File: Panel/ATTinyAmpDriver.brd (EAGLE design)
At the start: 50 x 50 mm, 44 parts, among them Q1 SI2301CDS, Q2 BC846, U1 SPX5205M5-L-3-3, U2 ATTINY5-TSHR, U3 MCP6L2-X_SN

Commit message: Turn and Tail combined Panel
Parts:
- removed LED10, LED11, LED12, LED5, LED6, LED7, LED8, LED9: LUXEON_REBELCREE_XP-E, Combined:CREE_XP-E
- removed X1, X2: (no value), con-phoenix-254:2POL254
- moved U$1 35.3 mm to (5.33, 7.92), turned to 90 degrees
- moved LED3 35.3 mm to (37.7, 13.2), flipped to the bottom, turned to 180 degrees
- moved Q1 35.0 mm to (31.1, 2.59), turned to 270 degrees
- moved C1 33.9 mm to (13.6, 3.63), turned to 180 degrees
- moved R2 33.2 mm to (25.5, 2.51), turned to 90 degrees
- moved R1 31.5 mm to (22.8, 3.58), turned to 0 degrees
- moved C6 31.3 mm to (19.1, 4.01), turned to 270 degrees
- moved PWM 31.1 mm to (29.1, 4.80), turned to 0 degrees
- moved TPIDATA 31.0 mm to (20.6, 4.01), turned to 0 degrees
- moved C3 30.9 mm to (16.8, 4.78), turned to 270 degrees
- moved Q2 30.3 mm to (27.1, 4.85), turned to 180 degrees
- moved U1 30.2 mm to (13.5, 6.53), turned to 0 degrees
- moved +5V 29.4 mm to (15.2, 6.48), turned to 0 degrees
- moved RESET 28.8 mm to (20.6, 5.61), turned to 0 degrees
- moved C5 27.7 mm to (23.5, 6.30), turned to 180 degrees
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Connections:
- removed net N$1 (its old number): LED5.AN, LED6.CT
- removed net N$13: LED11.CT, LED12.AN
- removed net N$14: LED9.AN, Q1.P$3
- removed net N$15: LED10.AN, LED9.CT
- removed net N$2 (its old number): LED1.AN, LED2.CT
- removed net N$4 (its old number): LED3.AN, LED4.CT
- removed net N$5 (its old number): LED6.AN, LED7.CT
- removed net N$6 (its old number): LED7.AN, LED8.CT
- removed net THERMAL: LED1.TH, LED2.TH, LED3.TH, LED4.TH
- removed net THERMAL1: LED5.TH, LED6.TH, LED7.TH, LED8.TH
- removed net V+: LED4.AN, X1.1
- removed net V+1: LED8.AN, X2.1
- removed net V-: LED1.CT, X1.2
- removed net V-1: LED5.CT, X2.2
- new net N$10: LED3.CT, LED4.AN
- new net N$7: LED1.CT, LED2.AN
- net CROSSOVER: now also LED2.CT, LED3.AN; no longer LED10.CT, LED11.AN
- net D-: now also LED4.CT; no longer LED12.CT
- net GND: now also LED1.TH, LED2.TH, LED3.TH, LED4.TH; no longer LED10.TH, LED11.TH, LED12.TH, LED9.TH
- net N$3: now also LED1.AN, Q1.P$3; no longer LED2.AN, LED3.CT
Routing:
- net N$1 (its old number): track 15.1 -> 0.00 mm
- net N$2 (its old number): track 15.1 -> 0.00 mm
- net N$5 (its old number): track 11.7 -> 0.00 mm
- net N$6 (its old number): track 11.6 -> 0.00 mm
- net N$4 (its old number): track 11.6 -> 0.00 mm
- net N$3: track 11.7 -> 4.97 mm
- net V+1: track 6.39 -> 0.00 mm
- net V+: track 6.39 -> 0.00 mm
- net V-: track 5.81 -> 0.00 mm
- net V-1: track 5.81 -> 0.00 mm
- net N$14: track 4.97 -> 0.00 mm
- net N$7: track 0.00 -> 4.76 mm, vias 0 -> 1
- net N$15: track 4.76 -> 0.00 mm, vias 1 -> 0
- net N$10: track 0.00 -> 4.06 mm, vias 0 -> 1
- net N$13: track 4.06 -> 0.00 mm, vias 1 -> 0
- removed copper zone on layer 1, net THERMAL
- removed copper zone on layer 16, net THERMAL
- removed copper zone on layer 1, net THERMAL1
- removed copper zone on layer 16, net THERMAL1
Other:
- board size 50 x 50 mm -> 41.9 x 15.9 mm
- board text removed: "+"
- board text removed: "-"
- board text removed: "EM20130714"

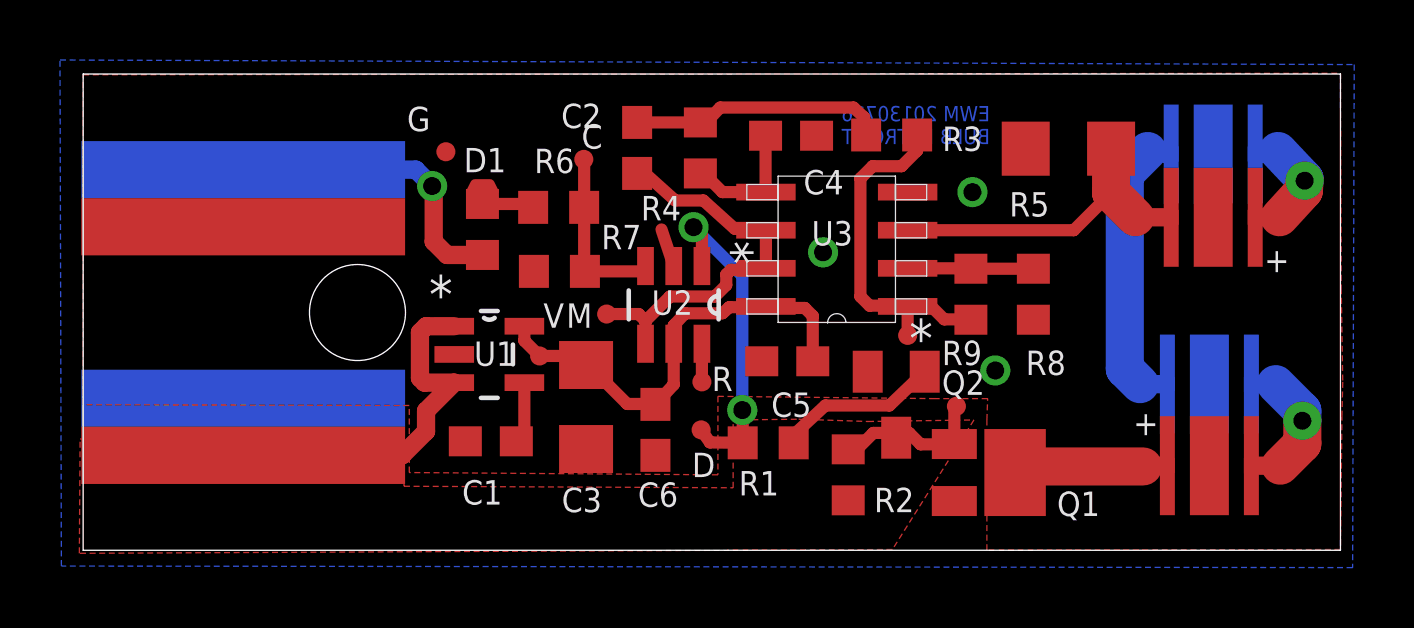
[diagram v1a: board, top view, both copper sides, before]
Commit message: updated tail board in combined panel
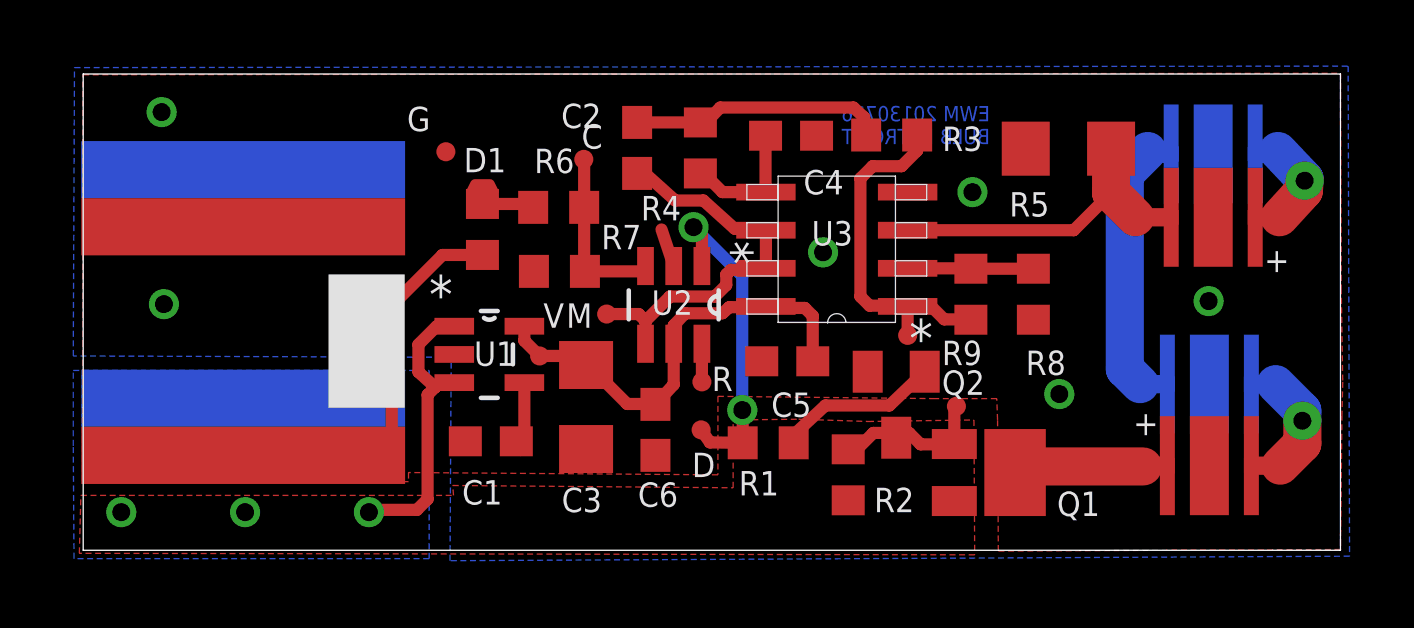
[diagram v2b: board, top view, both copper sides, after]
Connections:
- net +14V: now also U$1.L1; no longer U$1.H1
- net GND: now also U$1.H2; no longer U$1.L1
- net N$1: now also U$1.H1; no longer U$1.H2
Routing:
- net N$1: track 10.2 -> 13.6 mm, vias 1 -> 0
- net +14V: track 12.4 -> 9.79 mm, vias 0 -> 3
- net GND: vias 3 -> 6
- added copper zone on layer 16, net +14V
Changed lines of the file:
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@@
 <vertex x="41.9608" y="4.5212"/>
 <vertex x="41.91" y="0.0254"/>
-<vertex x="30.1244" y="0"/>
-<vertex x="30.1244" y="4.3434"/>
-<vertex x="30.1498" y="5.0546"/>
+<vertex x="30.5054" y="-0.0254"/>
+<vertex x="30.48" y="4.3434"/>
+<vertex x="30.4546" y="5.0546"/>
 <vertex x="28.3972" y="5.0546"/>
 <vertex x="21.1582" y="5.1308"/>
 <vertex x="21.1582" y="2.5146"/>
-<vertex x="10.8712" y="2.5908"/>
-<vertex x="10.8712" y="4.826"/>
-<vertex x="0" y="4.8514"/>
+<vertex x="10.8458" y="2.5908"/>
+<vertex x="10.8458" y="2.286"/>
+<vertex x="-0.0254" y="2.3114"/>
 </polygon>
 <polygon width="0.254" layer="16">
-<vertex x="-0.772" y="16.3422"/>
-<vertex x="42.369" y="16.1898"/>
-<vertex x="42.315" y="-0.5784"/>
-<vertex x="-0.726" y="-0.526"/>
+<vertex x="-0.2894" y="16.0882"/>
+<vertex x="42.1658" y="16.139"/>
+<vertex x="42.2134" y="-0.1974"/>
+<vertex x="12.228" y="-0.3482"/>
+<vertex x="12.2682" y="6.4336"/>
+<vertex x="-0.3302" y="6.477"/>
 </polygon>
 <contactref element="GND" pad="P$1"/>
@@
 <via x="24.6634" y="9.9314" extent="1-16" drill="0.6"/>
 <via x="29.6418" y="11.938" extent="1-16" drill="0.6"/>
-<via x="30.4038" y="5.9944" extent="1-16" drill="0.6"/>
+<via x="32.5374" y="5.207" extent="1-16" drill="0.6"/>
 <contactref element="LED1" pad="TH"/>
 <contactref element="LED4" pad="TH"/>
@@
 <contactref element="LED2" pad="TH"/>
 <contactref element="U$1" pad="L2"/>
-<contactref element="U$1" pad="L1"/>
+<contactref element="U$1" pad="H2"/>
+<via x="37.5158" y="8.3058" extent="1-16" drill="0.6"/>
+<via x="2.6162" y="14.605" extent="1-16" drill="0.6"/>
+<via x="2.6924" y="8.2042" extent="1-16" drill="0.6"/>
 </signal>
 <signal name="+14V">
@@
 <contactref element="U1" pad="3"/>
 <polygon width="0.254" layer="1">
-<vertex x="-0.1016" y="3.7084"/>
-<vertex x="10.7188" y="3.556"/>
-<vertex x="10.6934" y="2.1336"/>
+<vertex x="-0.0762" y="1.8288"/>
+<vertex x="12.3444" y="1.8288"/>
+<vertex x="12.319" y="2.159"/>
 <vertex x="21.6662" y="2.0828"/>
 <vertex x="21.6662" y="4.3434"/>
@@
 <vertex x="26.162" y="4.2926"/>
 <vertex x="29.6926" y="4.3434"/>
-<vertex x="26.9748" y="0.0254"/>
+<vertex x="29.718" y="-0.1524"/>
 <vertex x="-0.127" y="-0.1016"/>
 </polygon>
 <contactref element="Q1" pad="P$2"/>
 <contactref element="R2" pad="1"/>
-<contactref element="U$1" pad="H1"/>
-<wire x1="5.334" y1="3.1623" x2="10.6299" y2="3.1623" width="0.6096" layer="1"/>
-<wire x1="10.6299" y1="3.1623" x2="11.43" y2="3.9624" width="0.6096" layer="1"/>
-<wire x1="11.43" y1="3.9624" x2="11.43" y2="4.6482" width="0.6096" layer="1"/>
-<wire x1="11.43" y1="4.6482" x2="12.3698" y2="5.588" width="0.6096" layer="1"/>
-<wire x1="12.3698" y1="7.4676" x2="11.43" y2="7.4676" width="0.6096" layer="1"/>
-<wire x1="11.43" y1="7.4676" x2="11.2268" y2="7.2644" width="0.6096" layer="1"/>
-<wire x1="11.2268" y1="7.2644" x2="11.2268" y2="5.7404" width="0.6096" layer="1"/>
-<wire x1="11.2268" y1="5.7404" x2="11.3792" y2="5.588" width="0.6096" layer="1"/>
-<wire x1="11.3792" y1="5.588" x2="12.3698" y2="5.588" width="0.6096" layer="1"/>
-<wire x1="25.5016" y1="1.6646" x2="29.0392" y2="1.6408" width="0" layer="19" extent="1-1"/>
+<contactref element="U$1" pad="L1"/>
+<polygon width="0.3048" layer="16">
+<vertex x="-0.3302" y="5.9944"/>
+<vertex x="11.5316" y="5.9944"/>
+<vertex x="11.5316" y="-0.2794"/>
+<vertex x="-0.3048" y="-0.2794"/>
+<vertex x="-0.3302" y="3.4798"/>
+</polygon>
+<via x="1.27" y="1.27" extent="1-16" drill="0.6"/>
+<via x="5.3975" y="1.27" extent="1-16" drill="0.6"/>
+<via x="9.525" y="1.27" extent="1-16" drill="0.6"/>
+<wire x1="12.3698" y1="5.588" x2="11.8872" y2="5.588" width="0.4064" layer="1"/>
+<wire x1="11.8872" y1="5.588" x2="11.7348" y2="5.4356" width="0.4064" layer="1"/>
+<wire x1="11.7348" y1="5.4356" x2="11.4808" y2="5.1816" width="0.4064" layer="1"/>
+<wire x1="11.4808" y1="5.1816" x2="11.4808" y2="1.7018" width="0.4064" layer="1"/>
+<wire x1="11.4808" y1="1.7018" x2="11.1252" y2="1.3462" width="0.4064" layer="1"/>
+<wire x1="11.1252" y1="1.3462" x2="9.6012" y2="1.3462" width="0.4064" layer="1"/>
+<wire x1="9.6012" y1="1.3462" x2="9.525" y2="1.27" width="0.4064" layer="1"/>
+<wire x1="12.3698" y1="7.4676" x2="11.7856" y2="7.4676" width="0.4064" layer="1"/>
+<wire x1="11.7856" y1="7.4676" x2="11.176" y2="6.858" width="0.4064" layer="1"/>
+<wire x1="11.176" y1="6.858" x2="11.176" y2="5.9436" width="0.4064" layer="1"/>
+<wire x1="11.176" y1="5.9436" x2="11.7348" y2="5.4356" width="0.4064" layer="1"/>
 </signal>
 <signal name="VCC">
@@
 <signal name="N$1">
 <contactref element="D1" pad="1A"/>
-<contactref element="U$1" pad="H2"/>
-<via x="11.6332" y="12.1412" extent="1-16" drill="0.6" diameter="0.4064" shape="square"/>
-<wire x1="13.3096" y1="9.8434" x2="12.1276" y2="9.8434" width="0.6096" layer="1"/>
-<wire x1="12.1276" y1="9.8434" x2="11.684" y2="10.287" width="0.6096" layer="1"/>
-<wire x1="11.684" y1="10.287" x2="11.684" y2="12.0904" width="0.6096" layer="1"/>
-<wire x1="11.684" y1="12.0904" x2="11.6332" y2="12.1412" width="0.6096" layer="1"/>
-<wire x1="5.334" y1="12.6873" x2="11.0871" y2="12.6873" width="0.6096" layer="16"/>
-<wire x1="11.0871" y1="12.6873" x2="11.6332" y2="12.1412" width="0.6096" layer="16"/>
+<contactref element="U$1" pad="H1"/>
+<wire x1="13.3096" y1="9.8434" x2="11.977" y2="9.8434" width="0.4064" layer="1"/>
+<wire x1="11.977" y1="9.8434" x2="10.287" y2="8.1534" width="0.4064" layer="1"/>
+<wire x1="10.287" y1="8.1534" x2="10.287" y2="3.3528" width="0.4064" layer="1"/>
+<wire x1="10.287" y1="3.3528" x2="10.0584" y2="3.1242" width="0.4064" layer="1"/>
+<wire x1="10.0584" y1="3.1242" x2="5.3721" y2="3.1242" width="0.4064" layer="1"/>
+<wire x1="5.3721" y1="3.1242" x2="5.334" y2="3.1623" width="0.4064" layer="1"/>
 </signal>
 <signal name="N$4">
